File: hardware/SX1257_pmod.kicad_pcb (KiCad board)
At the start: 4 copper layers, 20.3 x 45.5 mm, 46 parts, among them J1 Conn_02x06_Odd_Even, J2 SMA_F_RX, J3 SMA_F_TX, U1 SX1257, U2 SC18IS602B, Y1 36MHz 10ppm

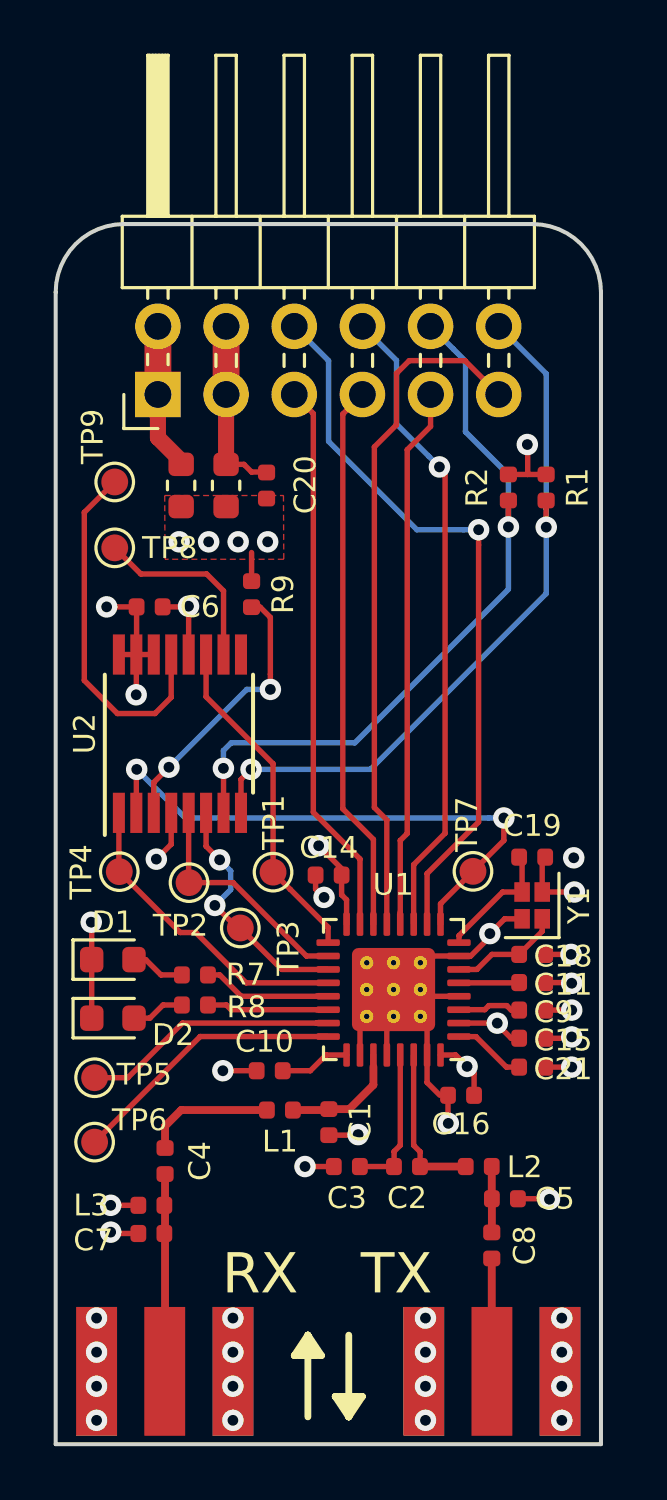
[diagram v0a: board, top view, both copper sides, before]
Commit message: Integrate SI514
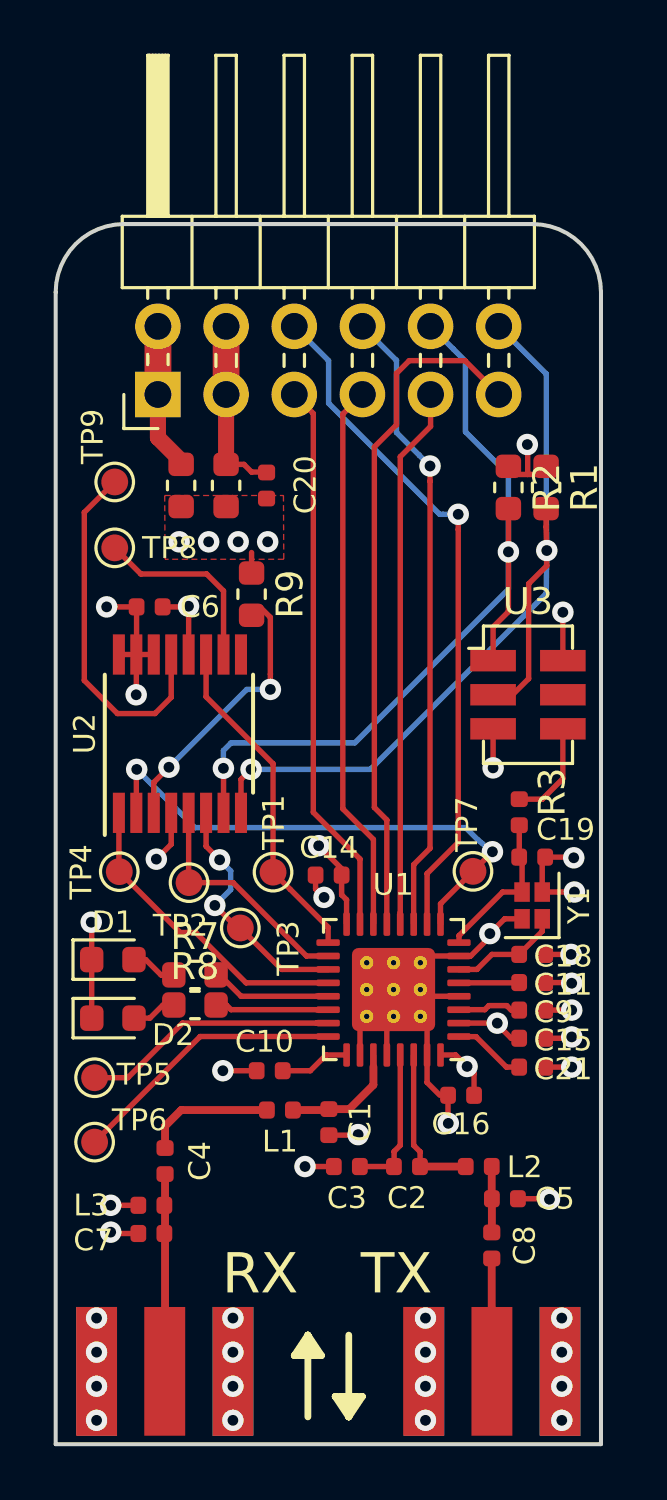
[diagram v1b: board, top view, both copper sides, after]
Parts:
- added R3: R, Resistor_SMD:R_0402_1005Metric, F.Cu at (131.6, 44.8)
- added U3: Si514, extra:Oscillator_SMD_Silicon_Labs_3.2x5.0mm_P1.27mm-6pin_5.0x3.2mm, F.Cu at (131.9, 40.4)
- R1, R2, R7, R8, R9: footprint Resistor_SMD:R_0402_1005Metric -> Resistor_SMD:R_0603_1608Metric
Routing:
- net /I2C_SCL: track 27.2 -> 34.7 mm
- net /I2C_SDA: track 27.4 -> 32.6 mm
- net Net-(R3-Pad2): track 0.00 -> 3.80 mm
- net GND: track 65.2 -> 67.8 mm, vias 36 -> 37
- net +3V3: track 14.6 -> 16.4 mm, vias 9 -> 10
- net /CLK_OUT: track 27.3 -> 25.7 mm
- net /SX_RESET: track 21.0 -> 19.6 mm
- net /XTB: track 4.47 -> 5.67 mm

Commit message: Fix resistors that accidentally reverted to 0603
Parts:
- R1, R2, R7, R8, R9: footprint Resistor_SMD:R_0603_1608Metric -> Resistor_SMD:R_0402_1005Metric

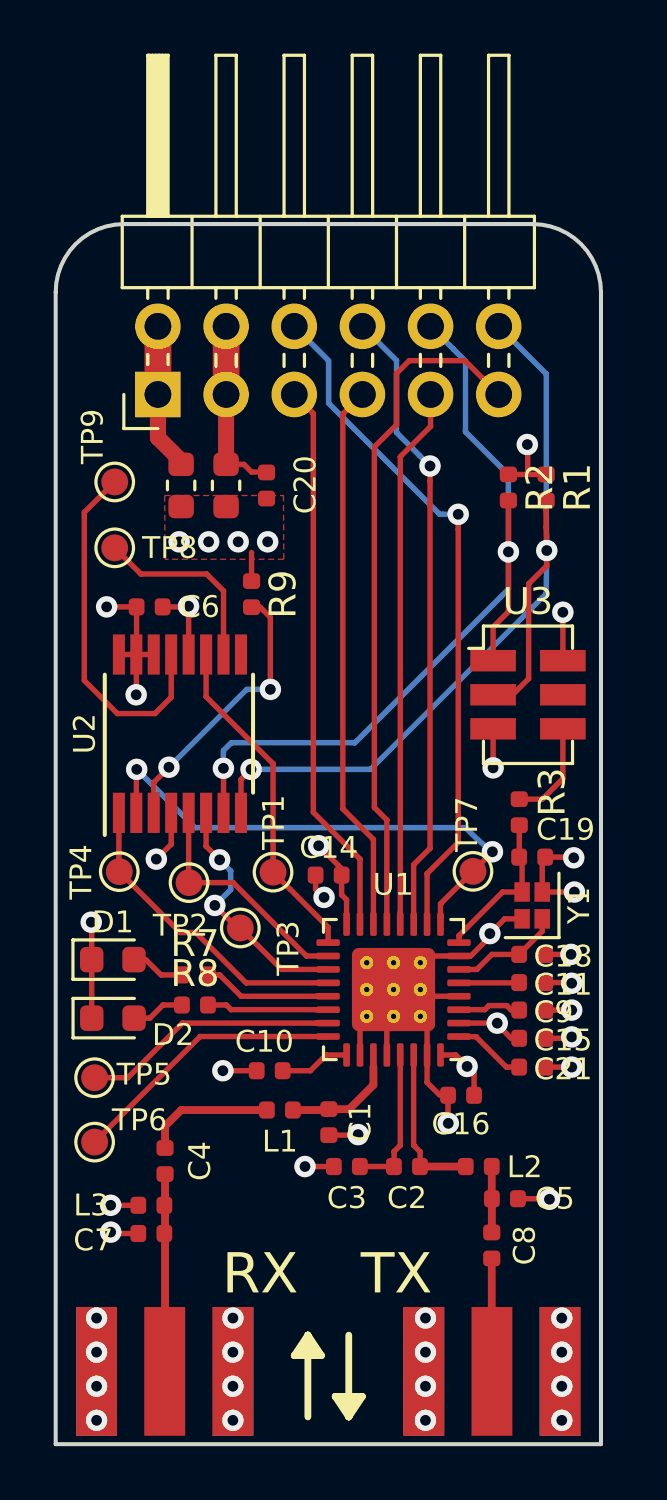
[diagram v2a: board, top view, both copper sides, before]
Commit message: Make SC18IS602B address pins accessible in case of rework
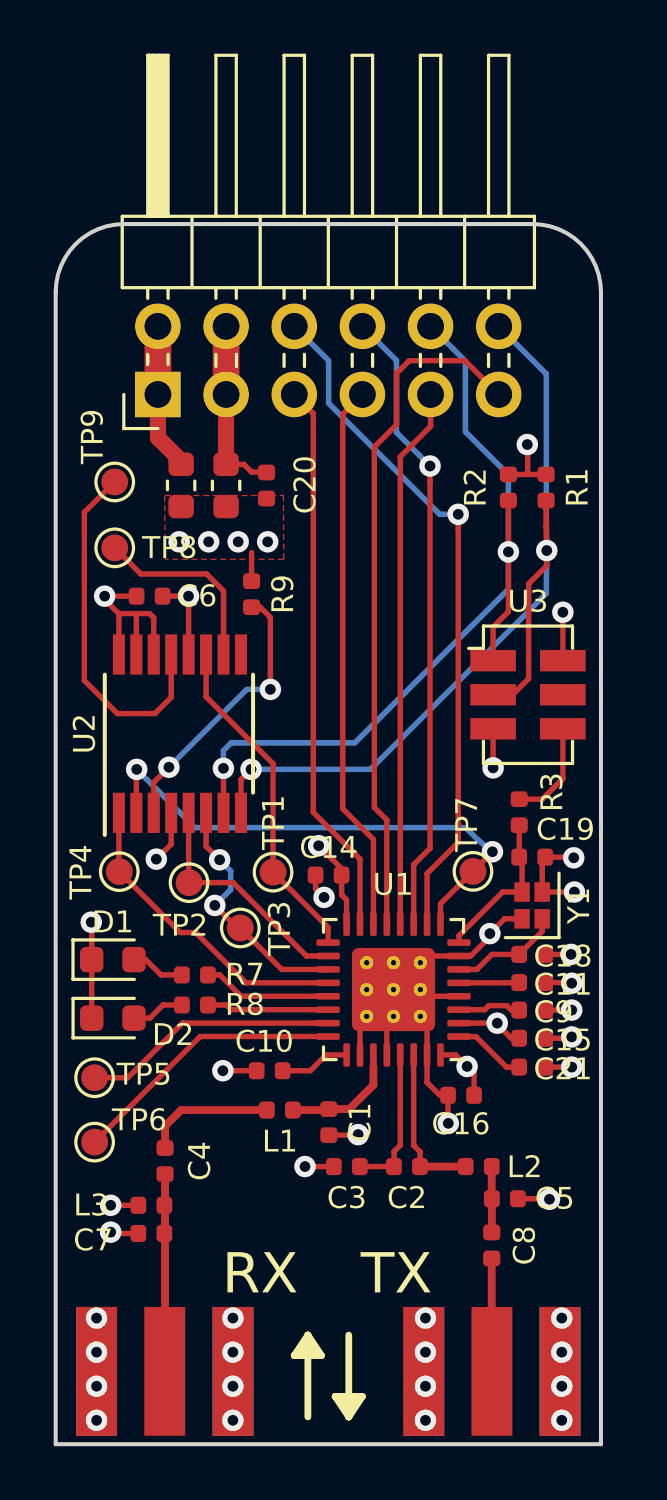
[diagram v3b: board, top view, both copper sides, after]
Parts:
- moved C6 0.40 mm to (117.8, 36.7)
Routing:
- net GND: track 67.8 -> 69.9 mm, vias 37 -> 36
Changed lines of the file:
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@@
     (thickness 1.6)
     (drawings 60)
-    (tracks 358)
+    (tracks 360)
     (zones 0)
     (modules 48)
@@
     (attr smd)
     (fp_text reference R9 (at 0 -1.17 90) (layer F.SilkS)
-      (effects (font (size 1 1) (thickness 0.15)))
+      (effects (font (size 0.8128 0.8128) (thickness 0.15)))
     )
     (fp_text value 10k (at 0 1.17 90) (layer F.Fab)
@@
     )
     (fp_text user %R (at 0 0 90) (layer F.Fab)
-      (effects (font (size 0.25 0.25) (thickness 0.04)))
+      (effects (font (size 0.8128 0.8128) (thickness 0.04)))
     )
     (fp_line (start 0.93 0.47) (end -0.93 0.47) (layer F.CrtYd) (width 0.05))
@@
     (tags resistor)
     (attr smd)
-    (fp_text reference R8 (at 0 -1.17) (layer F.SilkS)
-      (effects (font (size 1 1) (thickness 0.15)))
+    (fp_text reference R8 (at 1.86 -0.01) (layer F.SilkS)
+      (effects (font (size 0.8128 0.8128) (thickness 0.15)))
     )
     (fp_text value 2k (at 0 1.17) (layer F.Fab)
@@
     )
     (fp_text user %R (at 0 0) (layer F.Fab)
-      (effects (font (size 0.25 0.25) (thickness 0.04)))
+      (effects (font (size 0.8128 0.8128) (thickness 0.04)))
     )
     (fp_line (start 0.93 0.47) (end -0.93 0.47) (layer F.CrtYd) (width 0.05))
@@
     (tags resistor)
     (attr smd)
-    (fp_text reference R7 (at 0 -1.17) (layer F.SilkS)
-      (effects (font (size 1 1) (thickness 0.15)))
+    (fp_text reference R7 (at 1.86 -0.015) (layer F.SilkS)
+      (effects (font (size 0.8128 0.8128) (thickness 0.15)))
     )
     (fp_text value 2k (at 0 1.17) (layer F.Fab)
@@
     )
     (fp_text user %R (at 0 0) (layer F.Fab)
-      (effects (font (size 0.25 0.25) (thickness 0.04)))
+      (effects (font (size 0.8128 0.8128) (thickness 0.04)))
     )
     (fp_line (start 0.93 0.47) (end -0.93 0.47) (layer F.CrtYd) (width 0.05))
@@
     (tags resistor)
     (attr smd)
-    (fp_text reference R2 (at 0 -1.17 90) (layer F.SilkS)
-      (effects (font (size 1 1) (thickness 0.15)))
+    (fp_text reference R2 (at 0 1.22 90) (layer F.SilkS)
+      (effects (font (size 0.8128 0.8128) (thickness 0.15)))
     )
     (fp_text value 2k2 (at 0 1.17 90) (layer F.Fab)
@@
     )
     (fp_text user %R (at 0 0 90) (layer F.Fab)
-      (effects (font (size 0.25 0.25) (thickness 0.04)))
+      (effects (font (size 0.8128 0.8128) (thickness 0.04)))
     )
     (fp_line (start 0.93 0.47) (end -0.93 0.47) (layer F.CrtYd) (width 0.05))
@@
     (attr smd)
     (fp_text reference R1 (at 0 -1.17 90) (layer F.SilkS)
-      (effects (font (size 1 1) (thickness 0.15)))
+      (effects (font (size 0.8128 0.8128) (thickness 0.15)))
     )
     (fp_text value 2k2 (at 0 1.17 90) (layer F.Fab)
@@
     )
     (fp_text user %R (at 0 0 90) (layer F.Fab)
-      (effects (font (size 0.25 0.25) (thickness 0.04)))
+      (effects (font (size 0.8128 0.8128) (thickness 0.04)))
     )
     (fp_line (start 0.93 0.47) (end -0.93 0.47) (layer F.CrtYd) (width 0.05))
@@
     (attr smd)
     (fp_text reference U3 (at -3.475 0 180) (layer F.SilkS)
-      (effects (font (size 1 1) (thickness 0.15)))
+      (effects (font (size 0.8128 0.8128) (thickness 0.15)))
     )
     (fp_text value Si514 (at 0 3.15 90) (layer F.Fab)
@@
     (attr smd)
     (fp_text reference R3 (at 0.75 1.225 270) (layer F.SilkS)
-      (effects (font (size 1 1) (thickness 0.15)))
+      (effects (font (size 0.8128 0.8128) (thickness 0.15)))
     )
     (fp_text value R (at 0 1.17 90) (layer F.Fab)
@@
     (fp_line (start 0.93 0.47) (end -0.93 0.47) (layer F.CrtYd) (width 0.05))
     (fp_text user %R (at 0 0 90) (layer F.Fab)
-      (effects (font (size 0.25 0.25) (thickness 0.04)))
+      (effects (font (size 0.8128 0.8128) (thickness 0.04)))
     )
     (pad 1 smd roundrect (at -0.485 0 90) (size 0.59 0.64) (layers F.Cu F.Paste F.Mask) (roundrect_rratio 0.25)
@@
   )
   (module Capacitor_SMD:C_0402_1005Metric (layer F.Cu)
-    (at 117.8 37.125 180)
+    (at 117.8 36.725 180)
     (descr "Capacitor SMD 0402 (1005 Metric), square (rectangular) end terminal, IPC_7351 nominal, (Body size source: http://www.tortai-tech.com/upload/download/2011102023233369053.pdf), generated with kicad-footprint-generator")
     (tags capacitor)
     (attr smd)
-    (fp_text reference C6 (at -1.875 0) (layer F.SilkS)
+    (fp_text reference C6 (at -1.775 0) (layer F.SilkS)
       (effects (font (size 0.8128 0.8128) (thickness 0.15)))
     )
@@
     (tags "test point SMD pad")
     (attr virtual)
-    (fp_text reference TP3 (at -1.79 -0.75 270) (layer F.SilkS)
+    (fp_text reference TP3 (at -1.47 -0.01 270) (layer F.SilkS)
       (effects (font (size 0.8128 0.8128) (thickness 0.15)))
     )
@@
   (segment (start 120.634 31.8145) (end 121.3145 31.8145) (width 0.2032) (layer F.Cu) (net 1))
   (segment (start 121.3145 31.8145) (end 121.6 32.1) (width 0.2032) (layer F.Cu) (net 1))
-  (segment (start 116.655 38.9) (end 117.305 38.9) (width 0.2032) (layer F.Cu) (net 1))
-  (segment (start 117.955 38.9) (end 117.305 38.9) (width 0.2032) (layer F.Cu) (net 1))
-  (via (at 117.3 40.4) (size 0.8) (drill 0.4) (layers F.Cu B.Cu) (net 1))
-  (segment (start 117.305 38.9) (end 117.305 40.395) (width 0.2032) (layer F.Cu) (net 1))
-  (segment (start 117.305 40.395) (end 117.3 40.4) (width 0.2032) (layer F.Cu) (net 1))
   (via (at 132.7 59.2) (size 0.8) (drill 0.4) (layers F.Cu B.Cu) (net 1))
   (segment (start 131.525 59.18) (end 132.68 59.18) (width 0.2032) (layer F.Cu) (net 1))
@@
   (segment (start 123.985 47.12) (end 123.985 47.635) (width 0.2032) (layer F.Cu) (net 1))
   (segment (start 123.985 47.635) (end 124.3 47.95) (width 0.2032) (layer F.Cu) (net 1))
-  (segment (start 117.315 38.89) (end 117.305 38.9) (width 0.2032) (layer F.Cu) (net 1))
-  (segment (start 117.315 37.125) (end 117.315 38.89) (width 0.2032) (layer F.Cu) (net 1))
-  (via (at 116.2 37.125) (size 0.8) (drill 0.4) (layers F.Cu B.Cu) (net 1))
-  (segment (start 117.315 37.125) (end 116.2 37.125) (width 0.2032) (layer F.Cu) (net 1))
   (via (at 130.6 43.125) (size 0.8) (drill 0.4) (layers F.Cu B.Cu) (net 1))
   (segment (start 130.6 41.67) (end 130.6 43.125) (width 0.2032) (layer F.Cu) (net 1))
   (segment (start 133.58 46.45) (end 133.605 46.475) (width 0.2032) (layer F.Cu) (net 1))
   (segment (start 132.54 46.45) (end 133.58 46.45) (width 0.2032) (layer F.Cu) (net 1))
+  (via (at 116.125 36.725) (size 0.8) (drill 0.4) (layers F.Cu B.Cu) (net 1))
+  (segment (start 117.315 36.725) (end 116.125 36.725) (width 0.2032) (layer F.Cu) (net 1))
+  (segment (start 117.8 37.375) (end 117.955 37.53) (width 0.2032) (layer F.Cu) (net 1))
+  (segment (start 117.955 37.53) (end 117.955 38.9) (width 0.2032) (layer F.Cu) (net 1))
+  (segment (start 116.125 36.725) (end 116.125 36.85) (width 0.2032) (layer F.Cu) (net 1))
+  (segment (start 116.125 36.85) (end 116.65 37.375) (width 0.2032) (layer F.Cu) (net 1))
+  (segment (start 116.655 37.38) (end 116.655 38.9) (width 0.2032) (layer F.Cu) (net 1))
+  (segment (start 116.65 37.375) (end 116.655 37.38) (width 0.2032) (layer F.Cu) (net 1))
+  (segment (start 117.305 37.395) (end 117.305 38.9) (width 0.2032) (layer F.Cu) (net 1))
+  (segment (start 116.65 37.375) (end 117.325 37.375) (width 0.2032) (layer F.Cu) (net 1))
+  (segment (start 117.325 37.375) (end 117.305 37.395) (width 0.2032) (layer F.Cu) (net 1))
+  (segment (start 117.325 37.375) (end 117.8 37.375) (width 0.2032) (layer F.Cu) (net 1))
   (segment (start 129.3275 50.635) (end 129.995 50.635) (width 0.2032) (layer F.Cu) (net 2))
   (segment (start 130.555 50.075) (end 131.57 50.075) (width 0.2032) (layer F.Cu) (net 2))
@@
   (segment (start 131.17 32.19) (end 131.89 32.19) (width 0.2032) (layer F.Cu) (net 6))
   (segment (start 131.89 32.19) (end 132.575 32.19) (width 0.2032) (layer F.Cu) (net 6))
-  (segment (start 119.255 38.9) (end 119.255 37.105) (width 0.2032) (layer F.Cu) (net 6))
-  (segment (start 119.255 37.105) (end 119.25 37.1) (width 0.2032) (layer F.Cu) (net 6))
-  (segment (start 119.225 37.125) (end 119.25 37.1) (width 0.2032) (layer F.Cu) (net 6))
-  (via (at 119.25 37.1) (size 0.8) (drill 0.4) (layers F.Cu B.Cu) (net 6))
-  (segment (start 118.285 37.125) (end 119.225 37.125) (width 0.2032) (layer F.Cu) (net 6))
   (via (at 133.2 37.325) (size 0.8) (drill 0.4) (layers F.Cu B.Cu) (net 6))
   (segment (start 133.2 39.13) (end 133.2 37.325) (width 0.2032) (layer F.Cu) (net 6))
+  (via (at 119.249994 36.725) (size 0.8) (drill 0.4) (layers F.Cu B.Cu) (net 6))
+  (segment (start 118.285 36.725) (end 119.249994 36.725) (width 0.2032) (layer F.Cu) (net 6))
+  (segment (start 119.255 36.730006) (end 119.249994 36.725) (width 0.2032) (layer F.Cu) (net 6))
+  (segment (start 119.255 38.9) (end 119.255 36.730006) (width 0.2032) (layer F.Cu) (net 6))
   (segment (start 124.015 52.135) (end 124.4525 52.135) (width 0.2032) (layer F.Cu) (net 7))
   (segment (start 120.835 52.135) (end 124.015 52.135) (width 0.2032) (layer F.Cu) (net 7))

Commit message: Update silkscreen with new url and revision
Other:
- board text added: "SX1257 PMOD RevC 2020-01"
- board text added: "https://github.com/xil-se/SX1257-PMOD"
- board text removed: "SX1257 PMOD RevB 2019-05"
- board text removed: "https://git.xil.se/kbeckmann/SX1257"
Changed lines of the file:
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@@
-(kicad_pcb (version 20171130) (host pcbnew 5.1.5-52549c5~84~ubuntu18.04.1)
+(kicad_pcb (version 20171130) (host pcbnew 5.1.5)
   (general
     (thickness 1.6)
@@
   (gr_arc (start 132.08 25.4) (end 134.62 25.4) (angle -90) (layer Edge.Cuts) (width 0.15))
   (gr_arc (start 116.84 25.4) (end 116.84 22.86) (angle -90) (layer Edge.Cuts) (width 0.15))
-  (gr_text https://git.xil.se/kbeckmann/SX1257 (at 133 32.4 90) (layer B.SilkS)
+  (gr_text https://github.com/xil-se/SX1257-PMOD (at 133 28.4 90) (layer B.SilkS)
     (effects (font (size 1 1) (thickness 0.15)) (justify left mirror))
   )
@@
   (gr_line (start 127.508 27.432) (end 127 27.94) (layer B.SilkS) (width 0.254))
   (gr_line (start 130.048 27.432) (end 129.54 27.94) (layer B.SilkS) (width 0.254))
-  (gr_text "SX1257\nPMOD\nRevB\n2019-05" (at 124.4 56.896 90) (layer B.SilkS)
+  (gr_text "SX1257\nPMOD\nRevC\n2020-01" (at 124.4 56.896 90) (layer B.SilkS)
     (effects (font (size 1.5 1.5) (thickness 0.3)) (justify mirror))
   )
